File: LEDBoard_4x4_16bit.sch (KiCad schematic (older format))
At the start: 35 parts, among them J1 signal_in, J2 power, J6 signal_out, U1 TLC5971PWPR, U2 TLC5971PWPR, U3 TLC5971PWPR, U4 TLC5971PWPR

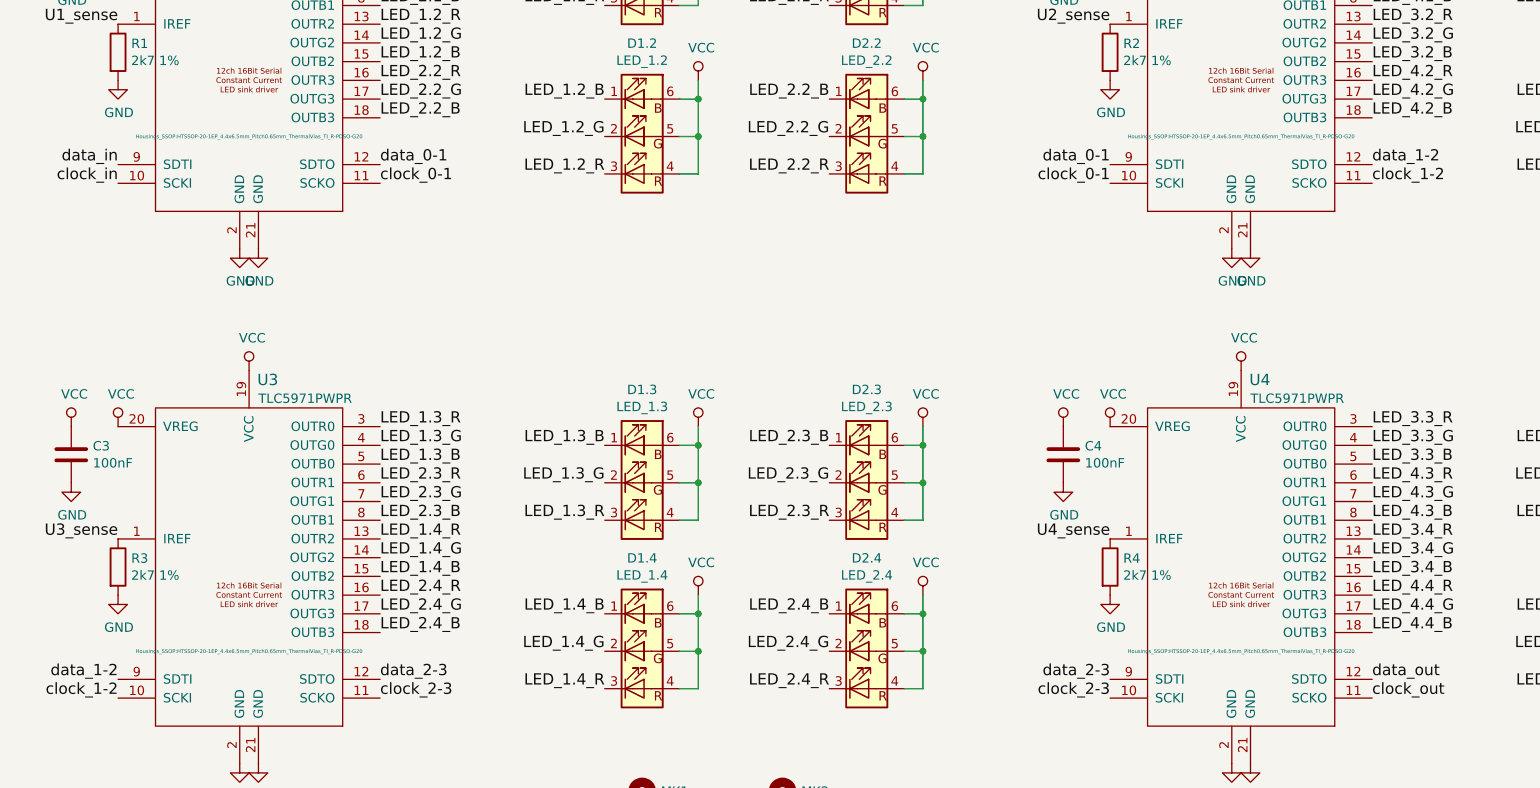
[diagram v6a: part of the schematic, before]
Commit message: updated smd pads to roundedrect version
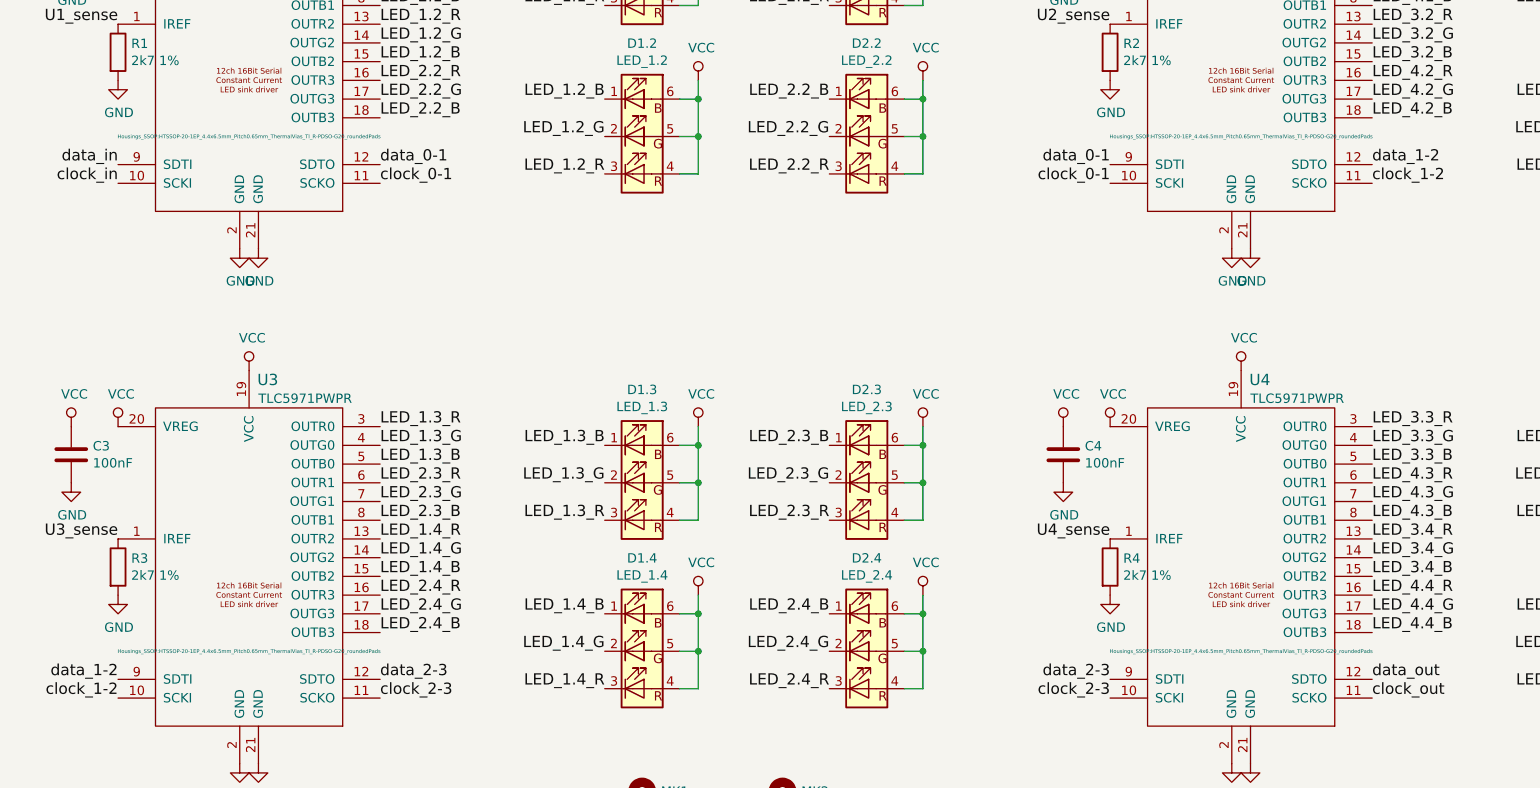
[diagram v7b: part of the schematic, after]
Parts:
- D1.1, D1.2, D1.3, D1.4, D2.1, D2.2, D2.3, D2.4, D3.1, D3.2, D3.3, D3.4, D4.1, D4.2, D4.3, D4.4: footprint nichia:LED_NSSM124_wViaHeatSinkBig -> nichia:LED_NSSM124_wViaHeatSinkBig_roundedPads
- U1, U2, U3, U4: footprint Housings_SSOP:HTSSOP-20-1EP_4.4x6.5mm_Pitch0.65mm_ThermalVias_TI_R-PDSO-G20 -> Housings_SSOP:HTSSOP-20-1EP_4.4x6.5mm_Pitch0.65mm_ThermalVias_TI_R-PDSO-G20_roundedPads
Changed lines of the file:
@@
 Sheet 1 1
 Title "LEDBoard 4x4 16bit"
-Date "31.08.2017"
-Rev "3.0.0"
+Date "27.09.2017"
+Rev "3.0.1"
 Comp "s-light.eu"
 Comment1 "designed by Stefan Krüger"
@@
 F 0 "D1.1" H 3950 2047 50  0000 C CNN
 F 1 "LED_1.1" H 3950 1956 50  0000 C CNN
-F 2 "nichia:LED_NSSM124_wViaHeatSinkBig" H 3950 1500 50  0001 C CNN
+F 2 "nichia:LED_NSSM124_wViaHeatSinkBig_roundedPads" H 3950 1500 50  0001 C CNN
 F 3 "" H 3950 1500 50  0001 C CNN
 F 4 "NSSM124D" H 3950 1550 60  0001 C CNN "Nichia part"
@@
 F 0 "U1" H 1950 3000 60  0000 C CNN
 F 1 "TLC5971PWPR" H 2150 2900 50  0000 C CNN
-F 2 "Housings_SSOP:HTSSOP-20-1EP_4.4x6.5mm_Pitch0.65mm_ThermalVias_TI_R-PDSO-G20" H 1850 1550 20  0000 C CNN
+F 2 "Housings_SSOP:HTSSOP-20-1EP_4.4x6.5mm_Pitch0.65mm_ThermalVias_TI_R-PDSO-G20_roundedPads" H 1850 1550 20  0000 C CNN
 F 3 "http://www.ti.com/product/TLC5971/description" H 1800 2000 60  0001 C CNN
 F 4 "595-TLC5971PWPR" H 1850 2000 60  0001 C CNN "mouser"
@@
 F 0 "D1.2" H 3950 2947 50  0000 C CNN
 F 1 "LED_1.2" H 3950 2856 50  0000 C CNN
-F 2 "nichia:LED_NSSM124_wViaHeatSinkBig" H 3950 2400 50  0001 C CNN
+F 2 "nichia:LED_NSSM124_wViaHeatSinkBig_roundedPads" H 3950 2400 50  0001 C CNN
 F 3 "" H 3950 2400 50  0001 C CNN
 F 4 "NSSM124D" H 3950 2450 60  0001 C CNN "Nichia part"
@@
 F 0 "D2.1" H 5150 2047 50  0000 C CNN
 F 1 "LED_2.1" H 5150 1956 50  0000 C CNN
-F 2 "nichia:LED_NSSM124_wViaHeatSinkBig" H 5150 1500 50  0001 C CNN
+F 2 "nichia:LED_NSSM124_wViaHeatSinkBig_roundedPads" H 5150 1500 50  0001 C CNN
 F 3 "" H 5150 1500 50  0001 C CNN
 F 4 "NSSM124D" H 5150 1550 60  0001 C CNN "Nichia part"
@@
 F 0 "D2.2" H 5150 2947 50  0000 C CNN
 F 1 "LED_2.2" H 5150 2856 50  0000 C CNN
-F 2 "nichia:LED_NSSM124_wViaHeatSinkBig" H 5150 2400 50  0001 C CNN
+F 2 "nichia:LED_NSSM124_wViaHeatSinkBig_roundedPads" H 5150 2400 50  0001 C CNN
 F 3 "" H 5150 2400 50  0001 C CNN
 F 4 "NSSM124D" H 5150 2450 60  0001 C CNN "Nichia part"
@@
 F 0 "D3.1" H 9250 2047 50  0000 C CNN
 F 1 "LED_3.1" H 9250 1956 50  0000 C CNN
-F 2 "nichia:LED_NSSM124_wViaHeatSinkBig" H 9250 1500 50  0001 C CNN
+F 2 "nichia:LED_NSSM124_wViaHeatSinkBig_roundedPads" H 9250 1500 50  0001 C CNN
 F 3 "" H 9250 1500 50  0001 C CNN
 F 4 "NSSM124D" H 9250 1550 60  0001 C CNN "Nichia part"
@@
 F 0 "D3.2" H 9250 2947 50  0000 C CNN
 F 1 "LED_3.2" H 9250 2856 50  0000 C CNN
-F 2 "nichia:LED_NSSM124_wViaHeatSinkBig" H 9250 2400 50  0001 C CNN
+F 2 "nichia:LED_NSSM124_wViaHeatSinkBig_roundedPads" H 9250 2400 50  0001 C CNN
 F 3 "" H 9250 2400 50  0001 C CNN
 F 4 "NSSM124D" H 9250 2450 60  0001 C CNN "Nichia part"
@@
 F 0 "D4.1" H 10450 2047 50  0000 C CNN
 F 1 "LED_4.1" H 10450 1956 50  0000 C CNN
-F 2 "nichia:LED_NSSM124_wViaHeatSinkBig" H 10450 1500 50  0001 C CNN
+F 2 "nichia:LED_NSSM124_wViaHeatSinkBig_roundedPads" H 10450 1500 50  0001 C CNN
 F 3 "" H 10450 1500 50  0001 C CNN
 F 4 "NSSM124D" H 10450 1550 60  0001 C CNN "Nichia part"
@@
 F 0 "D4.2" H 10450 2947 50  0000 C CNN
 F 1 "LED_4.2" H 10450 2856 50  0000 C CNN
-F 2 "nichia:LED_NSSM124_wViaHeatSinkBig" H 10450 2400 50  0001 C CNN
+F 2 "nichia:LED_NSSM124_wViaHeatSinkBig_roundedPads" H 10450 2400 50  0001 C CNN
 F 3 "" H 10450 2400 50  0001 C CNN
 F 4 "NSSM124D" H 10450 2450 60  0001 C CNN "Nichia part"
@@
 F 0 "D1.3" H 3950 4797 50  0000 C CNN
 F 1 "LED_1.3" H 3950 4706 50  0000 C CNN
-F 2 "nichia:LED_NSSM124_wViaHeatSinkBig" H 3950 4250 50  0001 C CNN
+F 2 "nichia:LED_NSSM124_wViaHeatSinkBig_roundedPads" H 3950 4250 50  0001 C CNN
 F 3 "" H 3950 4250 50  0001 C CNN
 F 4 "NSSM124D" H 3950 4300 60  0001 C CNN "Nichia part"
@@
 F 0 "U3" H 1950 5750 60  0000 C CNN
 F 1 "TLC5971PWPR" H 2150 5650 50  0000 C CNN
-F 2 "Housings_SSOP:HTSSOP-20-1EP_4.4x6.5mm_Pitch0.65mm_ThermalVias_TI_R-PDSO-G20" H 1850 4300 20  0000 C CNN
+F 2 "Housings_SSOP:HTSSOP-20-1EP_4.4x6.5mm_Pitch0.65mm_ThermalVias_TI_R-PDSO-G20_roundedPads" H 1850 4300 20  0000 C CNN
 F 3 "" H 1800 4750 60  0000 C CNN
 F 4 "595-TLC5971PWPR" H 0   0   60  0001 C CNN "mouser"
@@
 F 0 "D1.4" H 3950 5697 50  0000 C CNN
 F 1 "LED_1.4" H 3950 5606 50  0000 C CNN
-F 2 "nichia:LED_NSSM124_wViaHeatSinkBig" H 3950 5150 50  0001 C CNN
+F 2 "nichia:LED_NSSM124_wViaHeatSinkBig_roundedPads" H 3950 5150 50  0001 C CNN
 F 3 "" H 3950 5150 50  0001 C CNN
 F 4 "NSSM124D" H 3950 5200 60  0001 C CNN "Nichia part"
@@
 F 0 "D2.3" H 5150 4797 50  0000 C CNN
 F 1 "LED_2.3" H 5150 4706 50  0000 C CNN
-F 2 "nichia:LED_NSSM124_wViaHeatSinkBig" H 5150 4250 50  0001 C CNN
+F 2 "nichia:LED_NSSM124_wViaHeatSinkBig_roundedPads" H 5150 4250 50  0001 C CNN
 F 3 "" H 5150 4250 50  0001 C CNN
 F 4 "NSSM124D" H 5150 4300 60  0001 C CNN "Nichia part"
@@
 F 0 "D2.4" H 5150 5697 50  0000 C CNN
 F 1 "LED_2.4" H 5150 5606 50  0000 C CNN
-F 2 "nichia:LED_NSSM124_wViaHeatSinkBig" H 5150 5150 50  0001 C CNN
+F 2 "nichia:LED_NSSM124_wViaHeatSinkBig_roundedPads" H 5150 5150 50  0001 C CNN
 F 3 "" H 5150 5150 50  0001 C CNN
 F 4 "NSSM124D" H 5150 5200 60  0001 C CNN "Nichia part"
@@
 F 0 "D3.3" H 9250 4797 50  0000 C CNN
 F 1 "LED_3.3" H 9250 4706 50  0000 C CNN
-F 2 "nichia:LED_NSSM124_wViaHeatSinkBig" H 9250 4250 50  0001 C CNN
+F 2 "nichia:LED_NSSM124_wViaHeatSinkBig_roundedPads" H 9250 4250 50  0001 C CNN
 F 3 "" H 9250 4250 50  0001 C CNN
 F 4 "NSSM124D" H 9250 4300 60  0001 C CNN "Nichia part"
@@
 F 0 "U4" H 7250 5750 60  0000 C CNN
 F 1 "TLC5971PWPR" H 7450 5650 50  0000 C CNN
-F 2 "Housings_SSOP:HTSSOP-20-1EP_4.4x6.5mm_Pitch0.65mm_ThermalVias_TI_R-PDSO-G20" H 7150 4300 20  0000 C CNN
+F 2 "Housings_SSOP:HTSSOP-20-1EP_4.4x6.5mm_Pitch0.65mm_ThermalVias_TI_R-PDSO-G20_roundedPads" H 7150 4300 20  0000 C CNN
 F 3 "" H 7100 4750 60  0000 C CNN
 F 4 "595-TLC5971PWPR" H 0   0   60  0001 C CNN "mouser"
@@
 F 0 "D3.4" H 9250 5697 50  0000 C CNN
 F 1 "LED_3.4" H 9250 5606 50  0000 C CNN
-F 2 "nichia:LED_NSSM124_wViaHeatSinkBig" H 9250 5150 50  0001 C CNN
+F 2 "nichia:LED_NSSM124_wViaHeatSinkBig_roundedPads" H 9250 5150 50  0001 C CNN
 F 3 "" H 9250 5150 50  0001 C CNN
 F 4 "NSSM124D" H 9250 5200 60  0001 C CNN "Nichia part"
@@
 F 0 "D4.3" H 10450 4797 50  0000 C CNN
 F 1 "LED_4.3" H 10450 4706 50  0000 C CNN
-F 2 "nichia:LED_NSSM124_wViaHeatSinkBig" H 10450 4250 50  0001 C CNN
+F 2 "nichia:LED_NSSM124_wViaHeatSinkBig_roundedPads" H 10450 4250 50  0001 C CNN
 F 3 "" H 10450 4250 50  0001 C CNN
 F 4 "NSSM124D" H 10450 4300 60  0001 C CNN "Nichia part"
@@
 F 0 "D4.4" H 10450 5697 50  0000 C CNN
 F 1 "LED_4.4" H 10450 5606 50  0000 C CNN
-F 2 "nichia:LED_NSSM124_wViaHeatSinkBig" H 10450 5150 50  0001 C CNN
+F 2 "nichia:LED_NSSM124_wViaHeatSinkBig_roundedPads" H 10450 5150 50  0001 C CNN
 F 3 "" H 10450 5150 50  0001 C CNN
 F 4 "NSSM124D" H 10450 5200 60  0001 C CNN "Nichia part"
@@
 F 0 "U2" H 7250 3000 60  0000 C CNN
 F 1 "TLC5971PWPR" H 7450 2900 50  0000 C CNN
-F 2 "Housings_SSOP:HTSSOP-20-1EP_4.4x6.5mm_Pitch0.65mm_ThermalVias_TI_R-PDSO-G20" H 7150 1550 20  0000 C CNN
+F 2 "Housings_SSOP:HTSSOP-20-1EP_4.4x6.5mm_Pitch0.65mm_ThermalVias_TI_R-PDSO-G20_roundedPads" H 7150 1550 20  0000 C CNN
 F 3 "" H 7100 2000 60  0000 C CNN
 F 4 "595-TLC5971PWPR" H 0   0   60  0001 C CNN "mouser"

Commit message: updated schematic to new file format
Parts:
- C1, C2, C3, C4, C5: symbol C -> device1:C
- D1.1, D1.2, D1.3, D1.4, D2.1, D2.2, D2.3, D2.4, D3.1, D3.2, D3.3, D3.4, D4.1, D4.2, D4.3, D4.4: symbol LED_BGR_DieOnCathodeSide -> led_bgr:LED_BGR_DieOnCathodeSide
- HS1: symbol Heatsink -> LEDBoard_4x4_16bit-rescue:Heatsink-RESCUE-LEDBoard_4x4_16bit
- J1, J6: symbol CONN_01X03 -> LEDBoard_4x4_16bit-rescue:CONN_01X03-RESCUE-LEDBoard_4x4_16bit
- J2: symbol CONN_01X06 -> LEDBoard_4x4_16bit-rescue:CONN_01X06-RESCUE-LEDBoard_4x4_16bit
- MK1, MK2: symbol Mounting_Hole_PAD -> LEDBoard_4x4_16bit-rescue:Mounting_Hole_PAD-RESCUE-LEDBoard_4x4_16bit
- R1, R2, R3, R4: symbol R -> device1:R
- U1, U2, U4: symbol TLC5971PWPR -> TI_TLC5971:TLC5971PWPR
- U3: symbol TLC5971PWPR -> TI_TLC5971:TLC5971
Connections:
- wire segments 74 -> 110
